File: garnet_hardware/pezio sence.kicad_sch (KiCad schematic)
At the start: 67 parts, among them J11 PZ2, J12 PZ1, J6 Conn_01x02_Pin, J7 Conn_01x02_Pin, U4 OPA1664PW, U5 TLV761

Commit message: added part numbers for H-bridge, started on PCB layout
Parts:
- C10, C20, C21, C22, C24, C25, C26, C27, C28, C29, C30, C31, C32, C4, C5, C6, C9: footprint (none) -> Capacitor_SMD:C_0603_1608Metric_Pad1.08x0.95mm_HandSolder
- C13, C14, C15, C16, C17, C18: footprint (none) -> Capacitor_SMD:C_0603_1608Metric
- J6, J7: now in the parts list
- R10, R11, R13, R14, R15, R17, R18, R19, R20, R21, R22, R23, R24, R25, R26, R27, R28, R29, R30, R31, R32, R33, R34, R35, R8, R9: footprint (none) -> Resistor_SMD:R_0603_1608Metric_Pad0.98x0.95mm_HandSolder
- U3, U6: value (none) -> MCP33141D-10; footprint (none) -> Package_SO:MSOP-10_3x3mm_P0.5mm
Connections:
- net GND: now also J12.1 (Pin_1)

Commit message: power frount end and sd card layed out on PCB
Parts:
- added D10, D7, D8, D9: D, Diode_SMD:D_0603_1608Metric_Pad1.05x0.95mm_HandSolder, symbol Device:D
- C11, C8: footprint (none) -> Capacitor_SMD:C_0603_1608Metric_Pad1.08x0.95mm_HandSolder
- C19, C23: footprint (none) -> Capacitor_Tantalum_SMD:CP_EIA-3216-10_Kemet-I_HandSolder
- D1, D2, D3, D4: footprint (none) -> Diode_SMD:D_0603_1608Metric_Pad1.05x0.95mm_HandSolder
- J11, J12: footprint (none) -> Connector_PinHeader_2.54mm:PinHeader_1x03_P2.54mm_Horizontal
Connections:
- net +3V3: now also D7.1 (K), D9.1 (K)
- net CNVST1: no longer R35.2
- net GND: now also D10.2 (A), D8.2 (A)
- net PZ_2_AMP1_N: now also U4.8; no longer U4.14
- net PZ_2_AMP1_P: now also U4.14; no longer U4.8
- net PZ_2_AMP2_N: now also U6.3 (IN+); no longer U6.4 (IN-)
- net PZ_2_AMP2_P: now also U6.4 (IN-); no longer U6.3 (IN+)
- net SCLK1: no longer R33.2
- net SDI1: no longer R34.2
- net SDO1: no longer C30.1, R32.2
- net at C8.2, R14.2, R15.1: now also U4.12 (+), D7.2 (A), D8.1 (K); no longer U4.10 (+)
- net at C11.2, R15.2, R17.1: now also U4.10 (+), D10.1 (K), D9.2 (A); no longer U4.12 (+)
- net at R22.2, R23.1: now also U4.9 (-); no longer U4.13 (-)
- net at R18.2, R19.1: now also U4.13 (-); no longer U4.9 (-)
- new net CNVST0: R35.2
- new net SCLK0: R33.2
- new net SDI0: R34.2
- new net SDO0: C30.1, R32.2
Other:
- moved on the sheet: C13, C16, C21, C22, C23, C24, C25, C26, C27, C28, R14, R15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

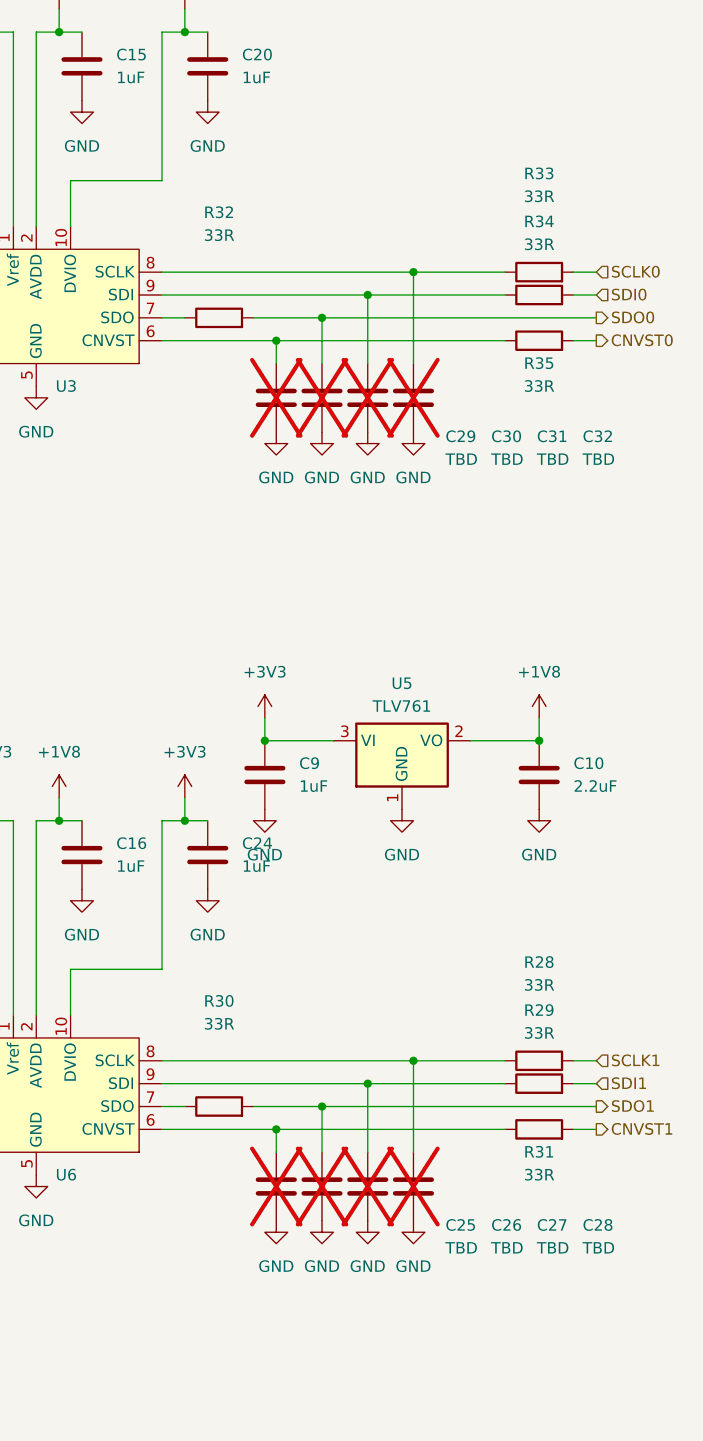
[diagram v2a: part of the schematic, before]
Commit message: cleaned SPI lines, replaced MOSFETS with more sutible ones, added free wheeling diodes added current sensing
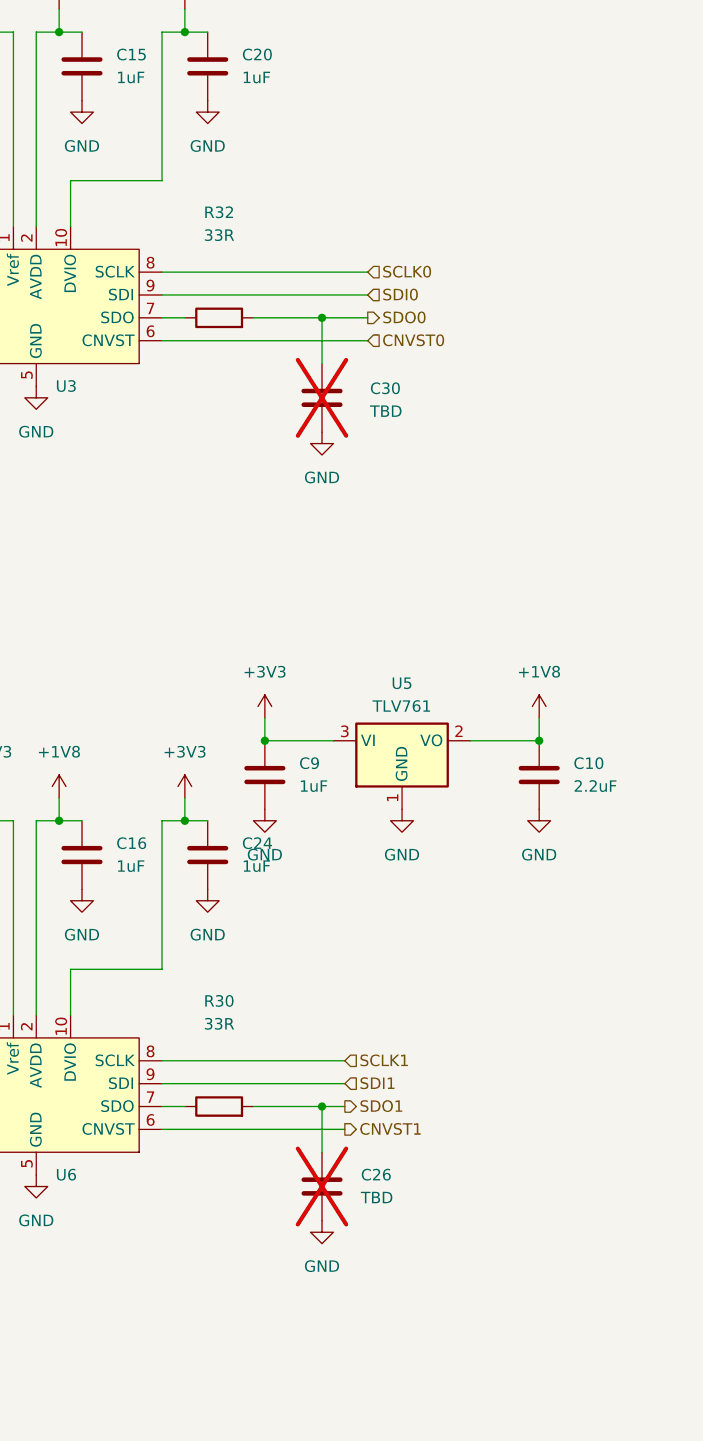
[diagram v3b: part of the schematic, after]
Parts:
- removed C25, C27, C28, C29, C31, C32: TBD, Capacitor_SMD:C_0603_1608Metric_Pad1.08x0.95mm_HandSolder, symbol Device:C
- removed R28, R29, R31, R33, R34, R35: 33R, Resistor_SMD:R_0603_1608Metric_Pad0.98x0.95mm_HandSolder, symbol Device:R
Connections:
- net CNVST0: now also U3.6 (CNVST)
- net CNVST1: now also U6.6 (CNVST)
- net SCLK0: now also U3.8 (SCLK)
- net SCLK1: now also U6.8 (SCLK)
- net SDI0: now also U3.9 (SDI)
- net SDI1: now also U6.9 (SDI)
